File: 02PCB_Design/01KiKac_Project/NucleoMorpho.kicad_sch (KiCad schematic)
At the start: 1 part, among them U11 NUCLEO-G431RB

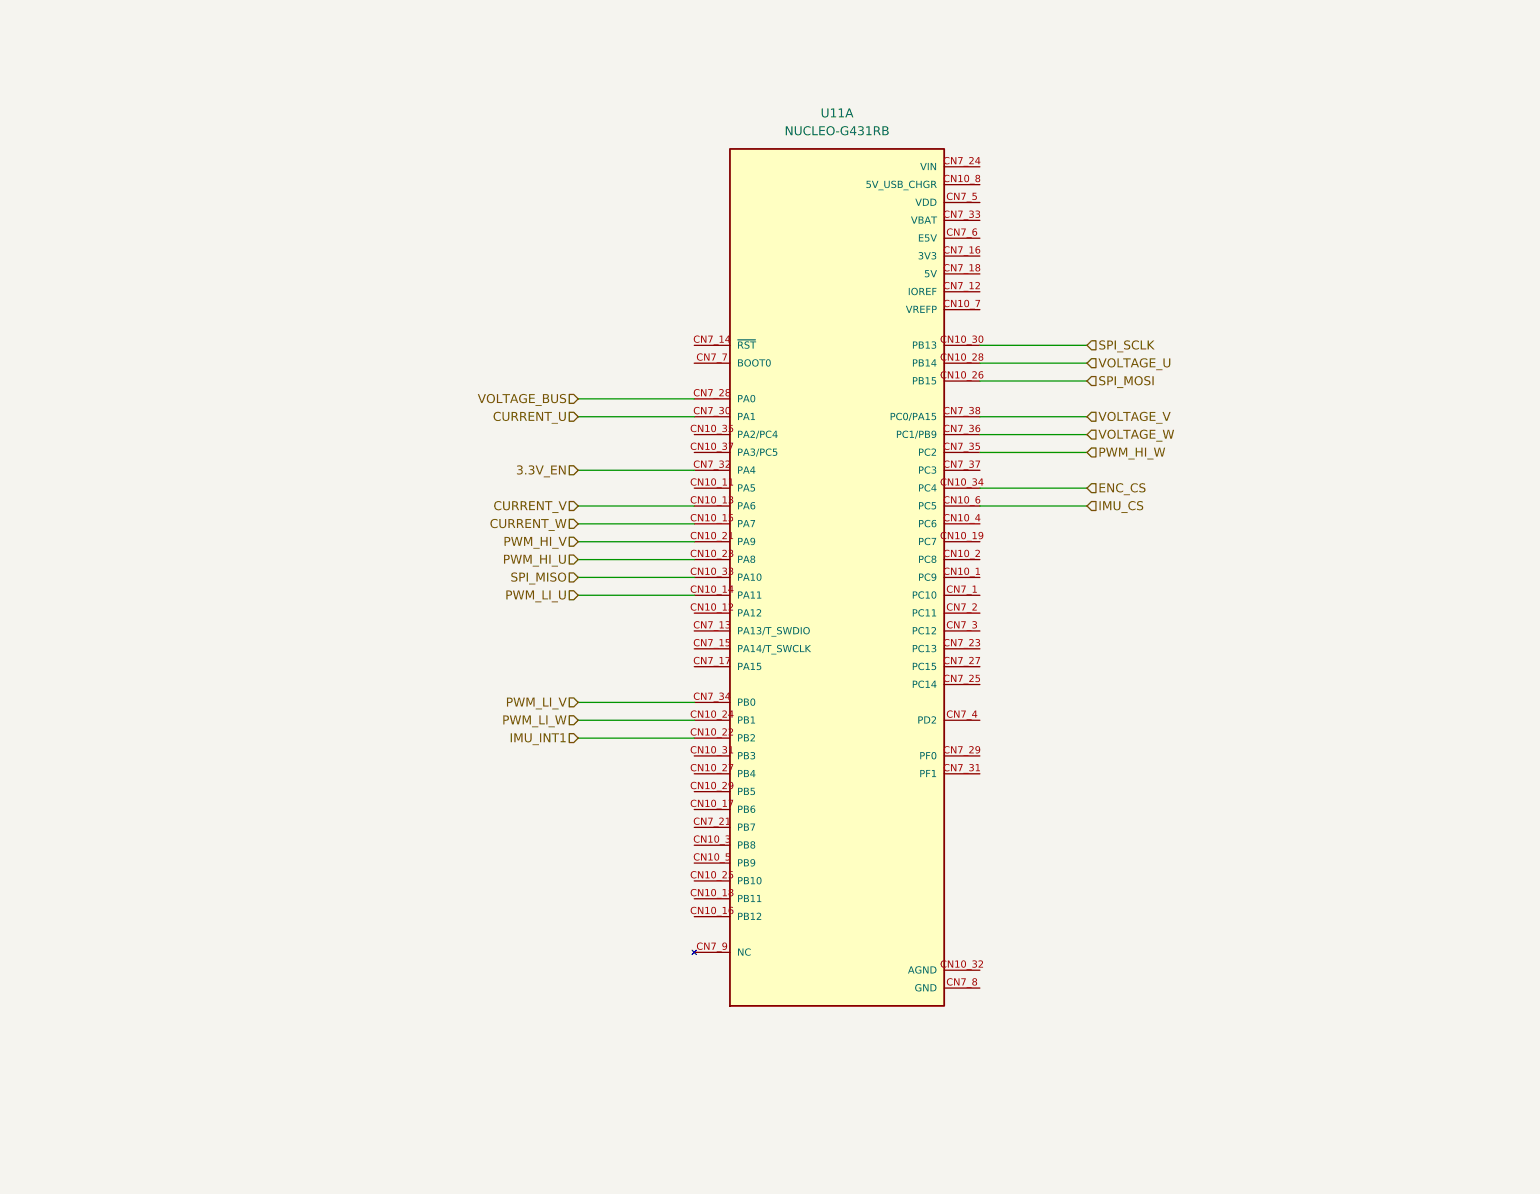
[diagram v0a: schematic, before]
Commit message: added CAN + minor changes
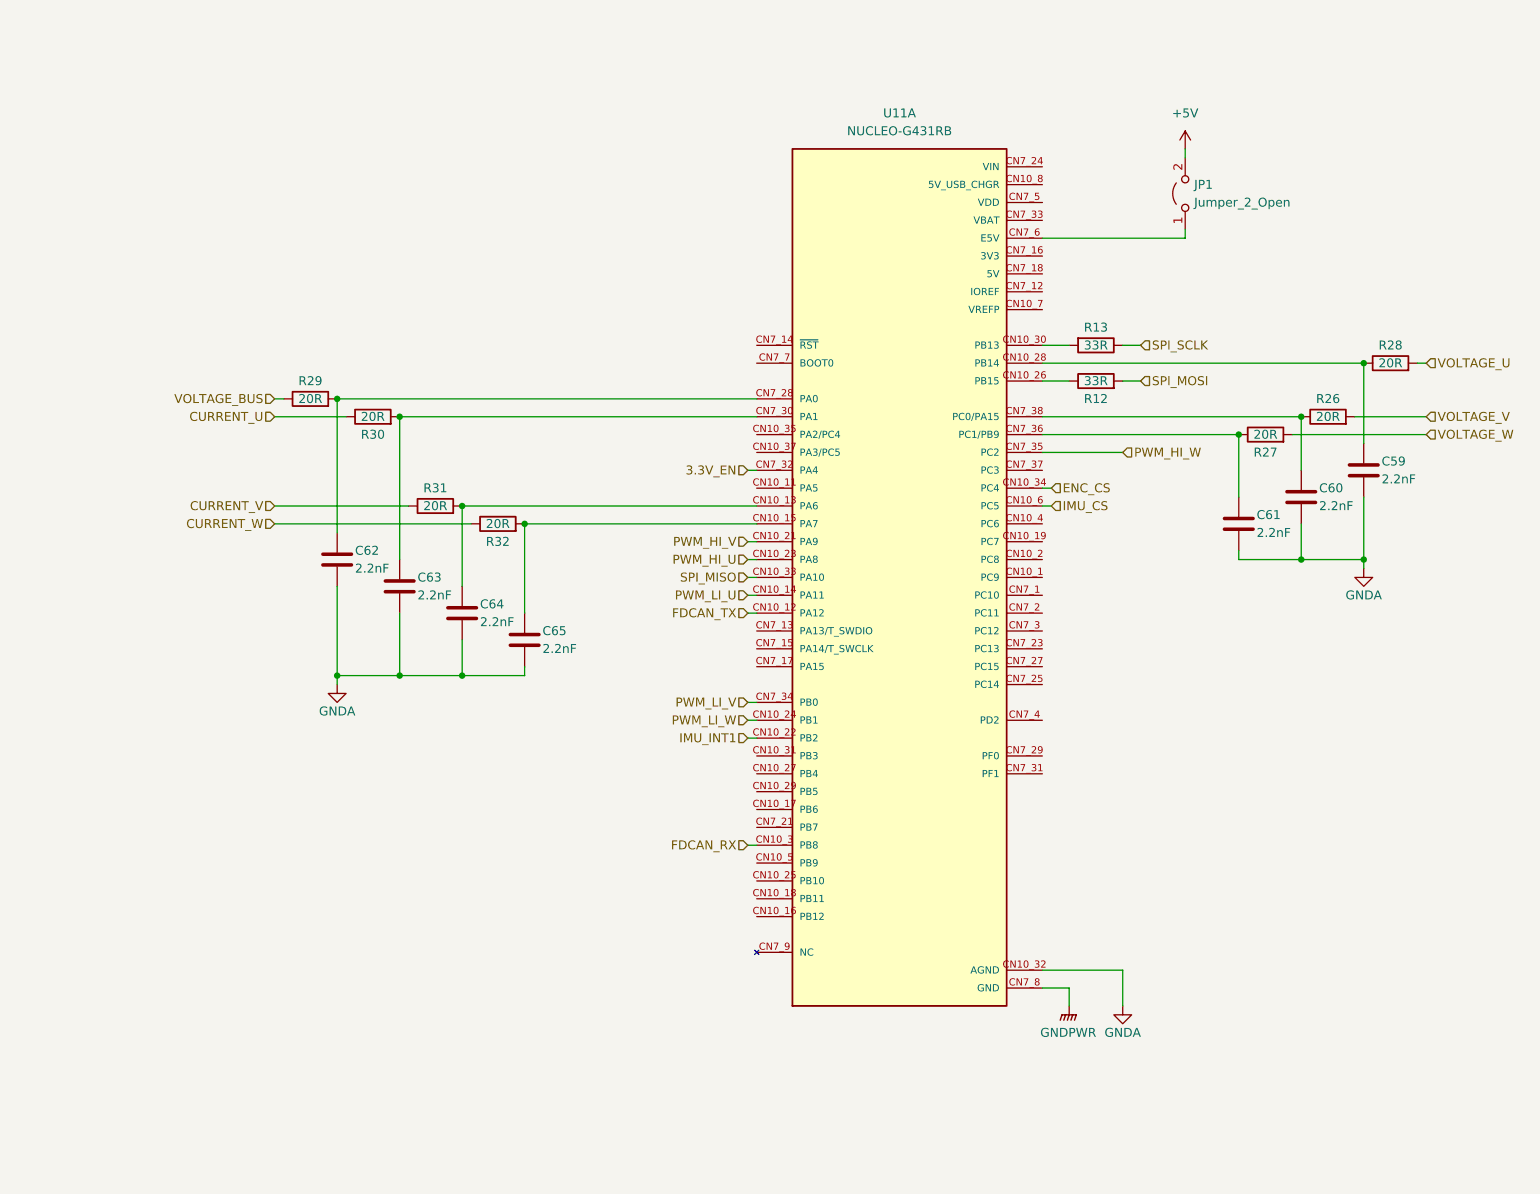
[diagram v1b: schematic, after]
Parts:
- added C59, C60, C61, C62, C63, C64, C65: 2.2nF, symbol Device:C
- added JP1: Jumper_2_Open, symbol Jumper:Jumper_2_Open
- added R12, R13: 33R, symbol Device:R
- added R26, R27, R28, R29, R30, R31, R32: 20R, symbol Device:R
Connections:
- net CURRENT_U: now also R30.1; no longer U11.CN7_30 (PA1)
- net CURRENT_V: now also R31.1; no longer U11.CN10_13 (PA6)
- net CURRENT_W: now also R32.1; no longer U11.CN10_15 (PA7)
- net SPI_MOSI: now also R12.2; no longer U11.CN10_26 (PB15)
- net SPI_SCLK: now also R13.1; no longer U11.CN10_30 (PB13)
- net VOLTAGE_BUS: now also R29.1; no longer U11.CN7_28 (PA0)
- net VOLTAGE_U: now also R28.2; no longer U11.CN10_28 (PB14)
- net VOLTAGE_V: now also R26.2; no longer U11.CN7_38 (PC0/PA15)
- net VOLTAGE_W: now also R27.2; no longer U11.CN7_36 (PC1/PB9)
- net FDCAN_TX: now reaches U11.CN10_12 (PA12)
- net FDCAN_RX: now reaches U11.CN10_3 (PB8)
- net GNDA: now reaches U11.CN10_32 (AGND)
- net GNDA: now also C59.2, C60.2, C61.2, C62.2, C63.2, C64.2, C65.2
- net at U11.CN7_6 (E5V): now also JP1.1 (A)
- new net: C61.1, R27.1, U11.CN7_36 (PC1/PB9)
- new net: C63.1, R30.2, U11.CN7_30 (PA1)
- new net: C60.1, R26.1, U11.CN7_38 (PC0/PA15)
- new net: R13.2, U11.CN10_30 (PB13)
- new net: R12.1, U11.CN10_26 (PB15)
- new net: C65.1, R32.2, U11.CN10_15 (PA7)
- new net: C64.1, R31.2, U11.CN10_13 (PA6)
- new net: C59.1, R28.1, U11.CN10_28 (PB14)
- new net: C62.1, R29.2, U11.CN7_28 (PA0)
- new net +5V: JP1.2 (B)
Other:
- moved on the sheet: U11A

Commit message: cleanup
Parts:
- removed JP1: Jumper_2_Open, symbol Jumper:Jumper_2_Open
- added JP1, JP2: SolderJumper_2_Bridged, symbol Jumper:SolderJumper_2_Bridged
- added JP3, JP4: SolderJumper_2_Open, symbol Jumper:SolderJumper_2_Open
- added R41, R42, R43: 33R, symbol Device:R
- renumbered C59 to C62, C60 to C63, C61 to C64, C62 to C65, C63 to C66, C64 to C67, C65 to C68, R13 to R31, R28 to R32, R12 to R33, R29 to R34, R30 to R35, R26 to R36, R27 to R37, R31 to R38, R32 to R39
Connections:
- net +5V: now also U11.CN7_6 (E5V)
- net FDCAN_RX: now also JP2.1 (A), JP3.1 (A); no longer U11.CN10_3 (PB8)
- net FDCAN_TX: now also JP1.1 (A), JP4.1 (A); no longer U11.CN10_12 (PA12)
- net PWM_LI_V: now also U11.CN10_12 (PA12); no longer U11.CN7_34 (PB0)
- net at C66.1, R35.2, U11.CN7_30 (PA1): now also U11.CN7_34 (PB0)
- net at U11.CN10_17 (PB6): now also R43.1
- net at U11.CN10_19 (PC7): now also R42.1
- net at U11.CN10_4 (PC6): now also R41.2
- net at U11.CN10_5 (PB9): now also JP1.2 (B), JP3.2 (B)
- net +3.3V: now reaches U11.CN10_7 (VREFP)
- new net: JP2.2 (B), JP4.2 (B), U11.CN10_3 (PB8)
- new net O_ENC_A: R41.1
- new net O_ENC_B: R42.2
- new net O_ENC_I: R43.2
- no-connect marks 0 -> 34
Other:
- note added: "Hardware COMP for Overcurrent protection"
- note added: "STM32 Morpho Header"
- moved on the sheet: C62, C63, C64, C65, C66, C67, C68, R31, R32, R33, R34, R35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

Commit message: besprechung
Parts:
- renumbered JP2 to JP1, JP4 to JP2, JP1 to JP4, R41 to R40, R42 to R41, R43 to R42
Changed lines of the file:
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@@
   (symbol (lib_id "Device:R") (at 153.67 87.63 90) (unit 1)
     (in_bom yes) (on_board yes) (dnp no)
-    (property "Reference" "R42" (at 153.67 90.17 90)
+    (property "Reference" "R41" (at 153.67 90.17 90)
       (effects (font (size 1.27 1.27)))
     )
@@
       (project "Testplatine"
         (path "/de27a806-41f8-462d-8678-2476d523bbd9/a9fc49c7-f356-4c2b-bdd5-d12f8bcc20f7/ebab6d44-f8ac-40ef-9001-86e6207db3e6"
-          (reference "R42") (unit 1)
+          (reference "R41") (unit 1)
         )
       )
@@
   (symbol (lib_id "power:GNDPWR") (at 149.86 153.67 0) (unit 1)
     (in_bom yes) (on_board yes) (dnp no) (fields_autoplaced)
-    (property "Reference" "#PWR067" (at 149.86 158.75 0)
+    (property "Reference" "#PWR068" (at 149.86 158.75 0)
       (effects (font (size 1.27 1.27)) hide)
     )
@@
       (project "Testplatine"
         (path "/de27a806-41f8-462d-8678-2476d523bbd9/a9fc49c7-f356-4c2b-bdd5-d12f8bcc20f7/ebab6d44-f8ac-40ef-9001-86e6207db3e6"
-          (reference "#PWR067") (unit 1)
+          (reference "#PWR068") (unit 1)
         )
       )
@@
   (symbol (lib_id "Jumper:SolderJumper_2_Bridged") (at 77.47 130.81 0) (unit 1)
     (in_bom yes) (on_board yes) (dnp no)
-    (property "Reference" "JP2" (at 77.47 125.73 0)
+    (property "Reference" "JP1" (at 77.47 125.73 0)
       (effects (font (size 1.27 1.27)))
     )
@@
       (project "Testplatine"
         (path "/de27a806-41f8-462d-8678-2476d523bbd9/a9fc49c7-f356-4c2b-bdd5-d12f8bcc20f7/ebab6d44-f8ac-40ef-9001-86e6207db3e6"
-          (reference "JP2") (unit 1)
+          (reference "JP1") (unit 1)
         )
       )
@@
   (symbol (lib_id "Device:R") (at 99.06 125.73 270) (unit 1)
     (in_bom yes) (on_board yes) (dnp no)
-    (property "Reference" "R43" (at 99.06 123.19 90)
+    (property "Reference" "R42" (at 99.06 123.19 90)
       (effects (font (size 1.27 1.27)))
     )
@@
       (project "Testplatine"
         (path "/de27a806-41f8-462d-8678-2476d523bbd9/a9fc49c7-f356-4c2b-bdd5-d12f8bcc20f7/ebab6d44-f8ac-40ef-9001-86e6207db3e6"
-          (reference "R43") (unit 1)
+          (reference "R42") (unit 1)
         )
       )
@@
   (symbol (lib_id "Jumper:SolderJumper_2_Bridged") (at 77.47 157.48 0) (unit 1)
     (in_bom yes) (on_board yes) (dnp no)
-    (property "Reference" "JP1" (at 77.47 152.4 0)
+    (property "Reference" "JP4" (at 77.47 152.4 0)
       (effects (font (size 1.27 1.27)))
     )
@@
       (project "Testplatine"
         (path "/de27a806-41f8-462d-8678-2476d523bbd9/a9fc49c7-f356-4c2b-bdd5-d12f8bcc20f7/ebab6d44-f8ac-40ef-9001-86e6207db3e6"
-          (reference "JP1") (unit 1)
+          (reference "JP4") (unit 1)
         )
       )
@@
   (symbol (lib_id "power:GNDA") (at 191.77 91.44 0) (unit 1)
     (in_bom yes) (on_board yes) (dnp no)
-    (property "Reference" "#PWR065" (at 191.77 97.79 0)
+    (property "Reference" "#PWR066" (at 191.77 97.79 0)
       (effects (font (size 1.27 1.27)) hide)
     )
@@
       (project "Testplatine"
         (path "/de27a806-41f8-462d-8678-2476d523bbd9/a9fc49c7-f356-4c2b-bdd5-d12f8bcc20f7/ebab6d44-f8ac-40ef-9001-86e6207db3e6"
-          (reference "#PWR065") (unit 1)
+          (reference "#PWR066") (unit 1)
         )
       )
@@
   (symbol (lib_id "Device:R") (at 153.67 85.09 270) (unit 1)
     (in_bom yes) (on_board yes) (dnp no)
-    (property "Reference" "R41" (at 153.67 82.55 90)
+    (property "Reference" "R40" (at 153.67 82.55 90)
       (effects (font (size 1.27 1.27)))
     )
@@
       (project "Testplatine"
         (path "/de27a806-41f8-462d-8678-2476d523bbd9/a9fc49c7-f356-4c2b-bdd5-d12f8bcc20f7/ebab6d44-f8ac-40ef-9001-86e6207db3e6"
-          (reference "R41") (unit 1)
+          (reference "R40") (unit 1)
         )
       )
@@
   (symbol (lib_id "power:+3.3V") (at 160.02 33.02 0) (unit 1)
     (in_bom yes) (on_board yes) (dnp no)
-    (property "Reference" "#PWR080" (at 160.02 36.83 0)
+    (property "Reference" "#PWR065" (at 160.02 36.83 0)
       (effects (font (size 1.27 1.27)) hide)
     )
@@
       (project "Testplatine"
         (path "/de27a806-41f8-462d-8678-2476d523bbd9/a9fc49c7-f356-4c2b-bdd5-d12f8bcc20f7/ebab6d44-f8ac-40ef-9001-86e6207db3e6"
-          (reference "#PWR080") (unit 1)
+          (reference "#PWR065") (unit 1)
         )
       )
@@
   (symbol (lib_id "power:GNDA") (at 45.72 107.95 0) (unit 1)
     (in_bom yes) (on_board yes) (dnp no)
-    (property "Reference" "#PWR066" (at 45.72 114.3 0)
+    (property "Reference" "#PWR067" (at 45.72 114.3 0)
       (effects (font (size 1.27 1.27)) hide)
     )
@@
       (project "Testplatine"
         (path "/de27a806-41f8-462d-8678-2476d523bbd9/a9fc49c7-f356-4c2b-bdd5-d12f8bcc20f7/ebab6d44-f8ac-40ef-9001-86e6207db3e6"
-          (reference "#PWR066") (unit 1)
+          (reference "#PWR067") (unit 1)
         )
       )
@@
   (symbol (lib_id "Jumper:SolderJumper_2_Open") (at 77.47 139.7 0) (unit 1)
     (in_bom yes) (on_board yes) (dnp no)
-    (property "Reference" "JP4" (at 77.47 134.62 0)
+    (property "Reference" "JP2" (at 77.47 134.62 0)
       (effects (font (size 1.27 1.27)))
     )
@@
       (project "Testplatine"
         (path "/de27a806-41f8-462d-8678-2476d523bbd9/a9fc49c7-f356-4c2b-bdd5-d12f8bcc20f7/ebab6d44-f8ac-40ef-9001-86e6207db3e6"
-          (reference "JP4") (unit 1)
+          (reference "JP2") (unit 1)
         )
       )
@@
   (symbol (lib_id "power:GNDA") (at 157.48 153.67 0) (unit 1)
     (in_bom yes) (on_board yes) (dnp no)
-    (property "Reference" "#PWR068" (at 157.48 160.02 0)
+    (property "Reference" "#PWR069" (at 157.48 160.02 0)
       (effects (font (size 1.27 1.27)) hide)
     )
@@
       (project "Testplatine"
         (path "/de27a806-41f8-462d-8678-2476d523bbd9/a9fc49c7-f356-4c2b-bdd5-d12f8bcc20f7/ebab6d44-f8ac-40ef-9001-86e6207db3e6"
-          (reference "#PWR068") (unit 1)
-        )
-      )
+          (reference "#PWR069") (unit 1)
+        )
+      )
